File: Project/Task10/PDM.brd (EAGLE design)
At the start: 100 x 80 mm, 44 parts

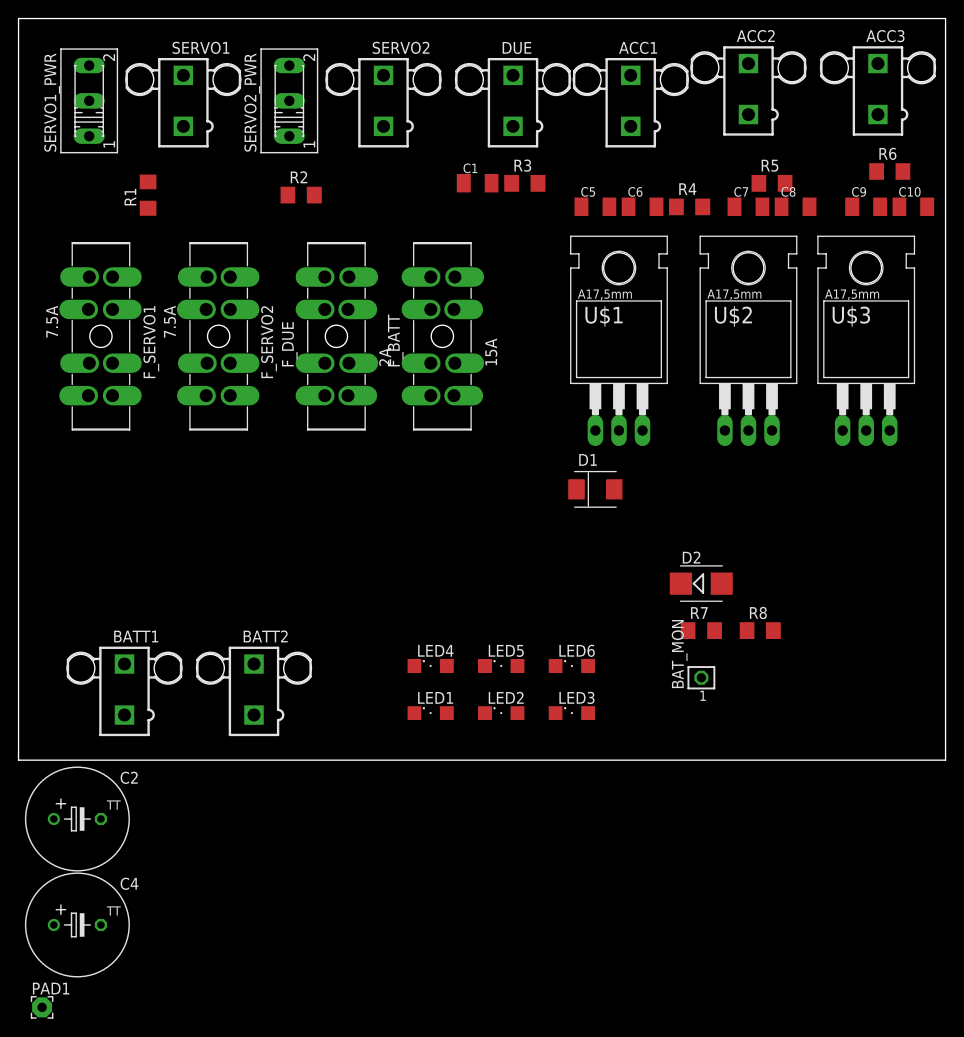
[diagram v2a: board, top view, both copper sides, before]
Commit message: Schematic and Board Updated
Schematic is updated with Battery Port XT60 and Caps.
Board is updated with basic placement, not yet routed
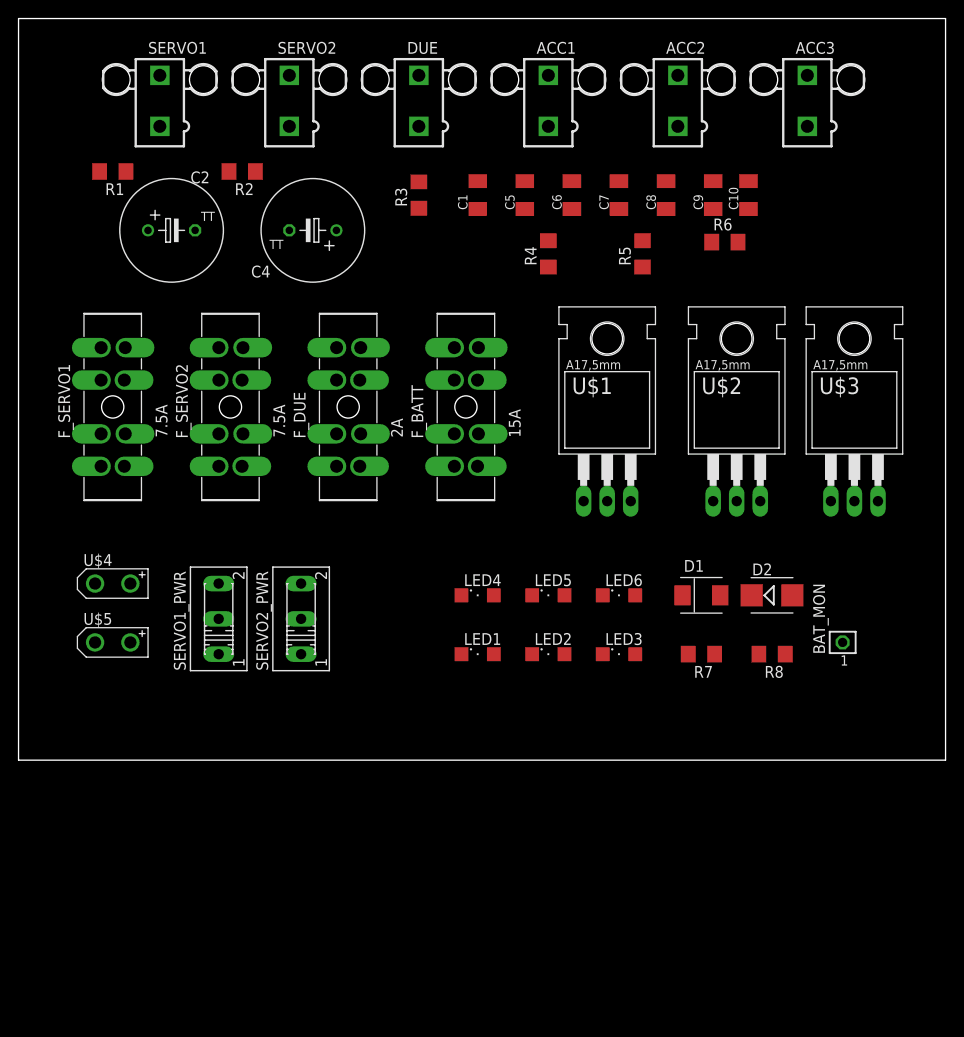
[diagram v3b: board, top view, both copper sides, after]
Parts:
- removed BATT1, BATT2: (no value), con-molex:5566-2
- removed PAD1: (no value), wirepad:2,15/1,0
- added U$4, U$5: CON_XT60-PIGTAIL, MRSDTeamB:CON_XT60_PIGTAIL
- moved C4 79.1 mm to (31.8, 57.1), turned to 180 degrees
- moved C2 64.3 mm to (16.5, 57.1)
- moved SERVO1_PWR 57.6 mm to (21.6, 15.2)
- moved SERVO2_PWR 55.9 mm to (30.5, 15.2)
- moved R6 19.3 mm to (76.2, 55.9)
- moved C10 17.8 mm to (78.7, 61.0), turned to 90 degrees
- moved C9 16.6 mm to (74.9, 61.0), turned to 90 degrees
- moved D1 16.2 mm to (73.7, 17.8)
- moved R4 16.1 mm to (57.1, 54.6), turned to 90 degrees
- moved R5 15.9 mm to (67.3, 54.6), turned to 90 degrees
- moved BAT_MON 15.7 mm to (88.9, 12.7)
- moved C7 14.0 mm to (64.8, 61.0), turned to 90 degrees
- moved C8 14.0 mm to (69.8, 61.0), turned to 90 degrees
- moved R3 11.5 mm to (43.2, 61.0), turned to 90 degrees
- moved DUE 10.2 mm to (43.2, 71.1)
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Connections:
- removed net N$10: BATT1.1, BATT2.1, F_BATT.A1, F_BATT.A2, F_BATT.A3, F_BATT.A4
- new net N$2: F_BATT.A1, F_BATT.A2, F_BATT.A3, F_BATT.A4, U$4.V+, U$5.V+
- net GND: now also U$4.V-, U$5.V-; no longer BATT1.2, BATT2.2
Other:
- board text added: "Acc1"
- board text added: "Acc2"
- board text added: "Acc3"
- board text added: "DUE"
- board text added: "Power"
- board text added: "SRV1"
- board text added: "SRV2"
- board text added: "Servo"
- board text added: "Status"

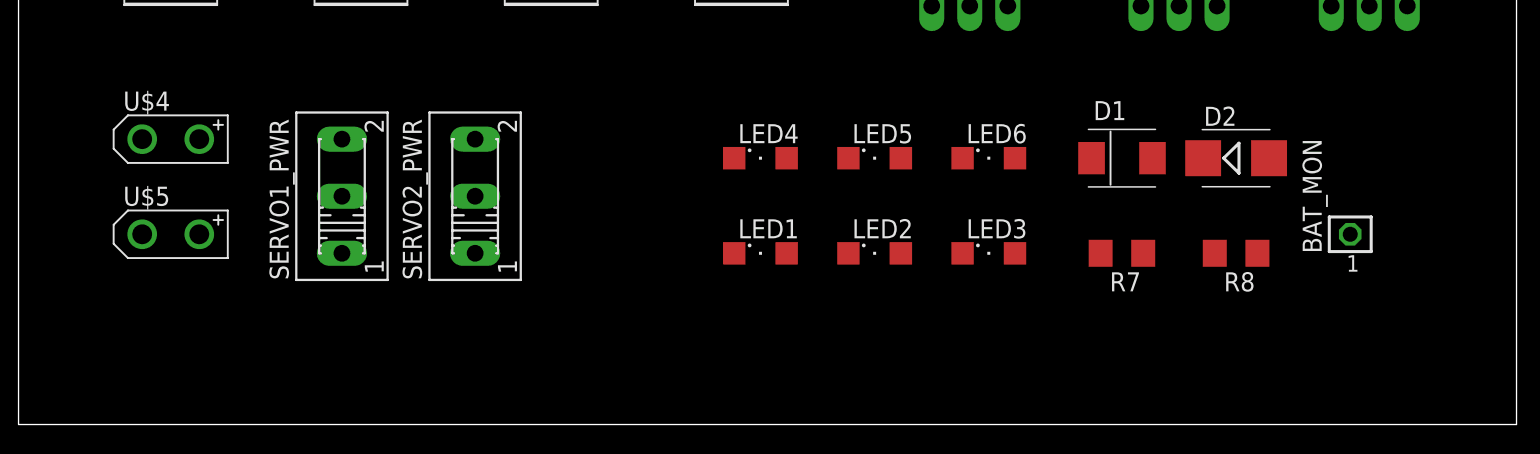
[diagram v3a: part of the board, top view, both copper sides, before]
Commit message: Datasheet for Power Switch 20A
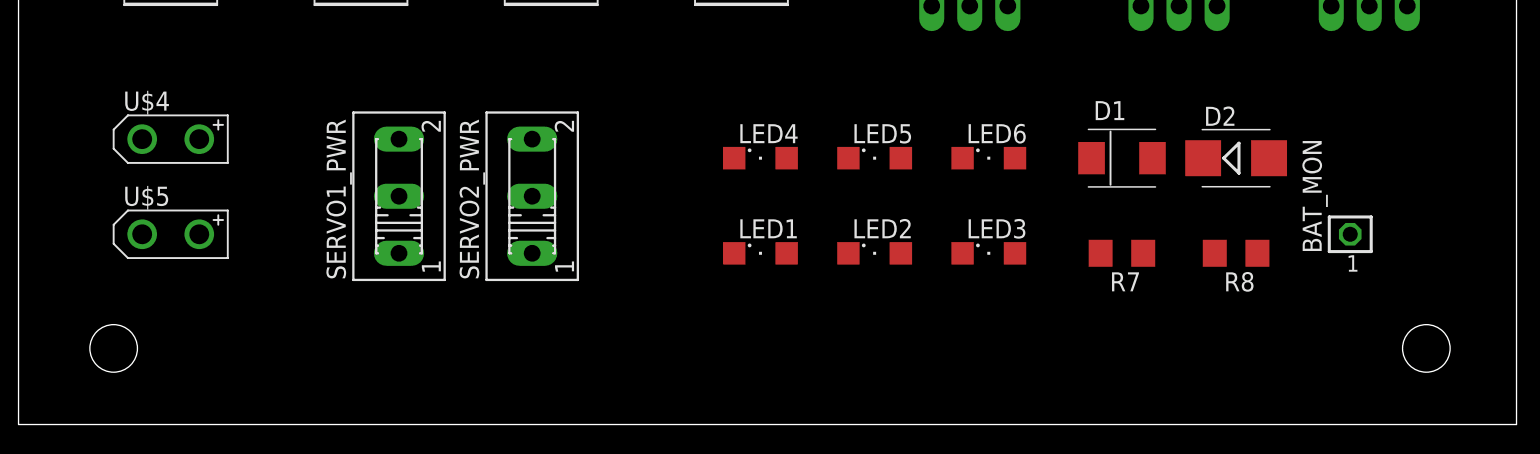
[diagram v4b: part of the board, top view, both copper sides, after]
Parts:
- moved SERVO1_PWR 3.81 mm to (25.4, 15.2)
- moved SERVO2_PWR 3.81 mm to (34.3, 15.2)
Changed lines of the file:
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@@
 <layer number="43" name="vRestrict" color="2" fill="10" visible="yes" active="yes"/>
 <layer number="44" name="Drills" color="7" fill="1" visible="no" active="yes"/>
-<layer number="45" name="Holes" color="7" fill="1" visible="no" active="yes"/>
+<layer number="45" name="Holes" color="7" fill="1" visible="yes" active="yes"/>
 <layer number="46" name="Milling" color="3" fill="1" visible="no" active="yes"/>
 <layer number="47" name="Measures" color="7" fill="1" visible="no" active="yes"/>
@@
 <wire x1="100" y1="80" x2="0" y2="80" width="0" layer="20"/>
 <wire x1="0" y1="80" x2="0" y2="0" width="0" layer="20"/>
-<text x="6.35" y="6.35" size="1.778" layer="104">Power</text>
-<text x="22.86" y="6.35" size="1.778" layer="104">Servo</text>
+<text x="7.62" y="8.89" size="1.778" layer="104">Power</text>
+<text x="26.67" y="6.35" size="1.778" layer="104">Servo</text>
 <text x="53.34" y="5.08" size="1.778" layer="104">Status</text>
 <wire x1="45.72" y1="21.59" x2="68.58" y2="21.59" width="0.4064" layer="104"/>
@@
 <text x="62.23" y="8.89" size="1.778" layer="104">Acc3</text>
 <wire x1="45.72" y1="7.62" x2="68.58" y2="7.62" width="0.4064" layer="104"/>
+<hole x="6.35" y="5.08" drill="3.175"/>
+<hole x="93.98" y="5.08" drill="3.175"/>
 </plain>
 <attributes>
@@
 <element name="C10" library="rcl" package="C1206K" value="10uF" x="78.74" y="60.96" rot="R90"/>
 <element name="C1" library="rcl" package="C1206K" value="10uF" x="49.53" y="60.96" rot="R90"/>
-<element name="SERVO1_PWR" library="switch" package="255SB" value="" x="21.59" y="15.24" rot="R90"/>
-<element name="SERVO2_PWR" library="switch" package="255SB" value="" x="30.48" y="15.24" rot="R90"/>
+<element name="SERVO1_PWR" library="switch" package="255SB" value="" x="25.4" y="15.24" rot="R90"/>
+<element name="SERVO2_PWR" library="switch" package="255SB" value="" x="34.29" y="15.24" rot="R90"/>
 <element name="D1" library="MRSDTeamB" package="SMBJ" value="8.5V" x="73.66" y="17.78"/>
 <element name="D2" library="diode" package="SMB" value="3.3V" x="81.28" y="17.78"/>
@@
 <contactref element="F_BATT" pad="B3"/>
 <contactref element="F_BATT" pad="B4"/>
-<wire x1="30.48" y1="15.24" x2="72.238" y2="11.43" width="0" layer="19" extent="1-1"/>
-<wire x1="54.61" y1="59.46" x2="30.48" y2="15.24" width="0" layer="19" extent="1-1"/>
+<wire x1="34.29" y1="15.24" x2="72.238" y2="11.43" width="0" layer="19" extent="1-1"/>
+<wire x1="54.61" y1="59.46" x2="34.29" y2="15.24" width="0" layer="19" extent="1-1"/>
 <wire x1="71.63" y1="17.78" x2="54.61" y2="59.46" width="0" layer="19" extent="1-1"/>
-<wire x1="21.59" y1="15.24" x2="72.238" y2="11.43" width="0" layer="19" extent="1-1"/>
+<wire x1="25.4" y1="15.24" x2="72.238" y2="11.43" width="0" layer="19" extent="1-1"/>
 <wire x1="69.85" y1="59.46" x2="71.63" y2="17.78" width="0" layer="19" extent="1-1"/>
 <wire x1="74.93" y1="59.46" x2="69.85" y2="59.46" width="0" layer="19" extent="1-1"/>
-<wire x1="34.31" y1="31.7" x2="30.48" y2="15.24" width="0" layer="19" extent="1-1"/>
+<wire x1="34.31" y1="31.7" x2="34.29" y2="15.24" width="0" layer="19" extent="1-1"/>
 <wire x1="36.81" y1="31.7" x2="34.31" y2="31.7" width="0" layer="19" extent="1-1"/>
 <wire x1="34.31" y1="35.2" x2="34.31" y2="31.7" width="0" layer="19" extent="1-1"/>
@@
 <contactref element="F_SERVO1" pad="A3"/>
 <contactref element="F_SERVO1" pad="A4"/>
-<wire x1="8.91" y1="35.2" x2="21.59" y2="11.43" width="0" layer="19" extent="1-1"/>
+<wire x1="8.91" y1="35.2" x2="25.4" y2="11.43" width="0" layer="19" extent="1-1"/>
 <wire x1="11.51" y1="35.2" x2="8.91" y2="35.2" width="0" layer="19" extent="1-1"/>
 <wire x1="8.91" y1="31.7" x2="8.91" y2="35.2" width="0" layer="19" extent="1-1"/>
@@
 <contactref element="F_SERVO2" pad="A3"/>
 <contactref element="F_SERVO2" pad="A4"/>
-<wire x1="21.61" y1="35.2" x2="30.48" y2="11.43" width="0" layer="19" extent="1-1"/>
+<wire x1="21.61" y1="35.2" x2="34.29" y2="11.43" width="0" layer="19" extent="1-1"/>
 <wire x1="24.21" y1="35.2" x2="21.61" y2="35.2" width="0" layer="19" extent="1-1"/>
 <wire x1="21.61" y1="31.7" x2="21.61" y2="35.2" width="0" layer="19" extent="1-1"/>

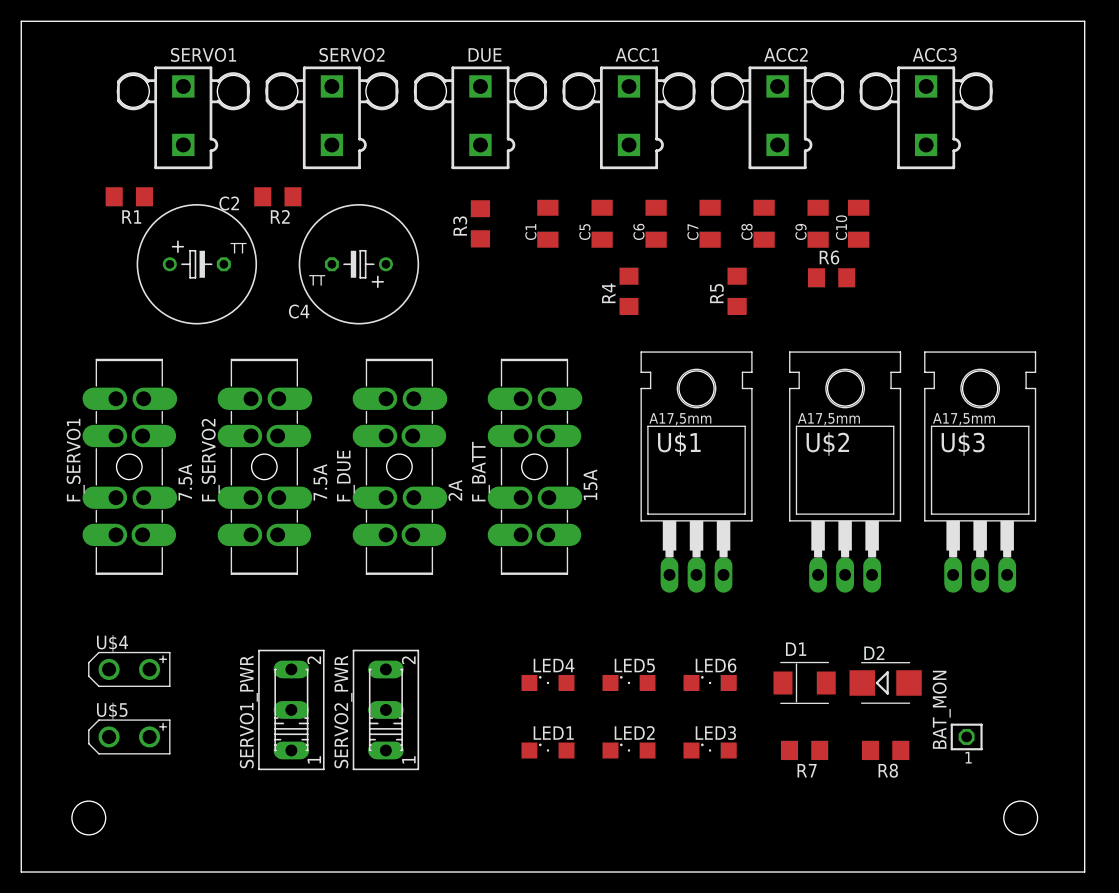
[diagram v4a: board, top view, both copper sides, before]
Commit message: Power Distribution Board Done, minus Power Switch
Mostly board design is done. Just need to add power switch.
The trace width is 423 mil, as calculated by the web
http://circuitcalculator.com/wordpress/?p=25/ , in order to deliver
current of 20A.
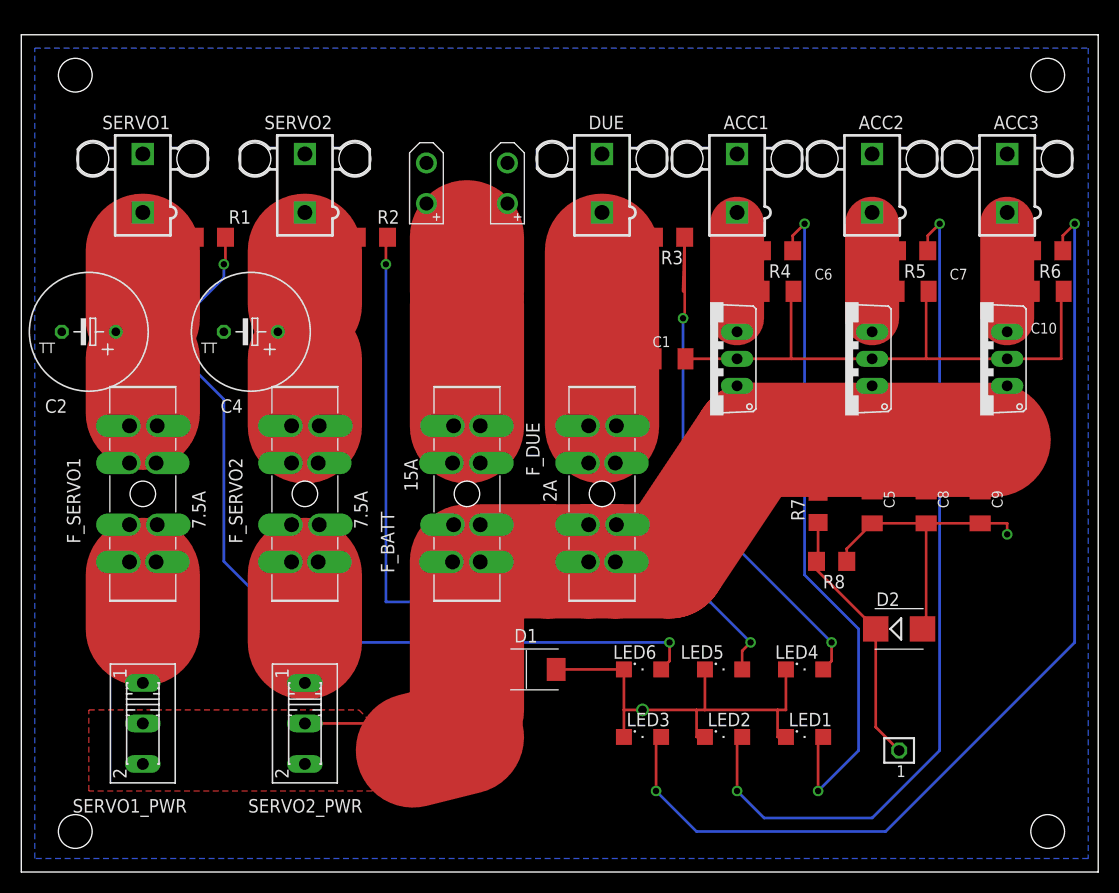
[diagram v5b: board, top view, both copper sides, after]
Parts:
- U$1, U$2, U$3: value MIC29150/29300/29500HORIZONTAL -> MIC29150/29300/29500VERTICAL; device MRSDTeamB:TO220H -> MRSDTeamB:TO220V
- moved U$5 59.1 mm to (38.1, 64.8), turned to 270 degrees
- moved U$4 57.9 mm to (45.7, 64.8), turned to 270 degrees
- moved C5 36.8 mm to (80.0, 34.3), turned to 270 degrees
- moved C8 30.7 mm to (85.1, 34.3), turned to 270 degrees
- moved C9 30.7 mm to (90.2, 34.3), turned to 270 degrees
- moved D1 25.4 mm to (48.3, 19.1)
- moved LED1 24.2 mm to (73.7, 12.7)
- moved LED4 24.2 mm to (73.7, 19.1)
- moved R7 22.9 mm to (74.9, 34.3), turned to 90 degrees
- moved R6 20.5 mm to (96.5, 58.4), turned to 180 degrees
- moved C7 20.1 mm to (83.8, 54.6), turned to 0 degrees
- moved F_DUE 19.2 mm to (54.6, 35.6)
- moved C10 18.9 mm to (96.5, 54.6), turned to 0 degrees
- moved R8 18.5 mm to (76.2, 29.2)
- moved R3 17.8 mm to (61.0, 59.7), turned to 180 degrees
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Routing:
- net V_SUPPLY: track 0.00 -> 151.4 mm
- net GND: track 0.00 -> 126.4 mm, vias 0 -> 2
- net N$22: track 0.00 -> 96.2 mm, vias 0 -> 2
- net N$5: track 0.00 -> 81.6 mm, vias 0 -> 2
- net N$16: track 0.00 -> 80.8 mm, vias 0 -> 2
- net N$29: track 0.00 -> 73.4 mm
- net N$8: track 0.00 -> 73.2 mm, vias 0 -> 2
- net N$13: track 0.00 -> 65.6 mm, vias 0 -> 2
- net N$11: track 0.00 -> 51.9 mm, vias 0 -> 2
- net N$4: track 0.00 -> 50.3 mm
- net N$15: track 0.00 -> 47.9 mm
- net N$1: track 0.00 -> 46.8 mm
- net N$2: track 0.00 -> 37.7 mm
- net N$18: track 0.00 -> 24.7 mm
- net N$14: track 0.00 -> 21.3 mm
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- added copper zone on layer 16, net GND
- added copper zone on layer 1, net V_SUPPLY
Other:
- board size 100 x 80 mm -> 101.3 x 78.7 mm
- board text added: "Battery"
- board text added: "Battery Monitoring"
- board text added: "Power Distribution Board - Team Space Jockey"
- board text removed: "Power"
- board text removed: "Servo"

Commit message: More PDM work
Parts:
- removed C4: (no value), rcl:TT5D11
- removed SERVO1_PWR, SERVO2_PWR: (no value), switch:255SB
- removed U$4, U$5: CON_XT60-PIGTAIL, MRSDTeamB:CON_XT60_PIGTAIL
- added BATT1, BATT2: (no value), MRSDTeamB:CON_XT60_PCB_MOUNT
- added BATT1_W, BATT2_W: (no value), MRSDTeamB:CON_XT60_PIGTAIL
- added C3: (no value), rcl:TT5D11
- moved R1 68.7 mm to (80.0, 30.5)
- moved R2 57.4 mm to (80.0, 26.7)
- moved R6 49.8 mm to (80.0, 11.4)
- moved R5 43.3 mm to (80.0, 15.2)
- moved R3 41.5 mm to (80.0, 22.9)
- moved R4 40.4 mm to (80.0, 19.1)
- moved D1 34.9 mm to (15.2, 7.62)
- moved F_BATT 32.8 mm to (15.2, 16.5), turned to 180 degrees
- moved LED3 29.7 mm to (86.4, 22.9), turned to 180 degrees
- moved C5 29.0 mm to (52.1, 41.9), turned to 90 degrees
- moved LED6 29.0 mm to (86.4, 11.4), turned to 180 degrees
- moved BAT_MON 28.0 mm to (61.0, 29.2)
- moved D2 26.7 mm to (55.9, 24.1), turned to 270 degrees
- moved LED2 24.7 mm to (86.4, 26.7), turned to 180 degrees
- moved C1 23.4 mm to (38.1, 53.3), turned to 180 degrees
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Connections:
- removed net N$12: F_SERVO1.A1, F_SERVO1.A2, F_SERVO1.A3, F_SERVO1.A4, SERVO1_PWR.1
- removed net N$14: F_SERVO2.A1, F_SERVO2.A2, F_SERVO2.A3, F_SERVO2.A4, SERVO2_PWR.1
- net GND: now also BATT1.V-, BATT1_W.V-, BATT2.V-, BATT2_W.V-, C3.-; no longer C4.-, U$4.V-, U$5.V-
- net N$1: now also C3.+; no longer C4.+
- net N$11: now also LED3.A; no longer LED4.A
- net N$13: now also LED4.A; no longer LED1.A
- net N$16: now also LED5.A; no longer LED2.A
- net N$2: now also BATT1.V+, BATT1_W.V+, BATT2.V+, BATT2_W.V+; no longer U$4.V+, U$5.V+
- net N$22: now also LED6.A; no longer LED3.A
- net N$5: now also LED1.A; no longer LED6.A
- net N$8: now also LED2.A; no longer LED5.A
- net N$9: now also C8.1; no longer C7.1
- net V_SUPPLY: now also C7.1, F_SERVO1.A1, F_SERVO1.A2, F_SERVO1.A3, F_SERVO1.A4, F_SERVO2.A1, F_SERVO2.A2, F_SERVO2.A3, F_SERVO2.A4; no longer C8.1, SERVO1_PWR.2, SERVO2_PWR.2
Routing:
- net V_SUPPLY: track 151.4 -> 0.00 mm
- net N$22: track 96.2 -> 3.18 mm, vias 2 -> 0
- net GND: track 126.4 -> 36.3 mm, vias 2 -> 0
- net N$5: track 81.6 -> 3.18 mm, vias 2 -> 0
- net N$16: track 80.8 -> 3.18 mm, vias 2 -> 0
- net N$29: track 73.4 -> 0.00 mm
- net N$8: track 73.2 -> 3.18 mm, vias 2 -> 0
- net N$13: track 65.6 -> 3.18 mm, vias 2 -> 0
- net N$4: track 50.3 -> 0.00 mm
- net N$11: track 51.9 -> 3.18 mm, vias 2 -> 0
- net N$15: track 47.9 -> 0.00 mm
- net N$1: track 46.8 -> 0.00 mm
- net N$2: track 37.7 -> 0.00 mm
- net N$14: track 21.3 -> 0.00 mm
- net N$12: track 21.2 -> 0.00 mm
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- added copper zone on layer 1, net GND
- added copper zone on layer 1, net N$1
- added copper zone on layer 1, net N$15
- added copper zone on layer 1, net N$2
- added copper zone on layer 1, net N$4
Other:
- board text added: "BATT MON"
- board text removed: "Acc1"
- board text removed: "Acc2"
- board text removed: "Acc3"
- board text removed: "Battery"
- board text removed: "Battery Monitoring"
- board text removed: "DUE"
- board text removed: "SRV1"
- board text removed: "SRV2"
